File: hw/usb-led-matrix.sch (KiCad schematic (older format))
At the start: 79 parts, among them J1 Conn_01x04_Male, J2 Conn_ARM_JTAG_SWD_10, J3 USB_A, U1 AP1117-33, U2 stm32g473, U3 74LVT244A, Y1 Crystal_GND23

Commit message: Updates
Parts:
- removed U3: 74LVT244A, Package_SO:SOIC-20W_7.5x12.8mm_P1.27mm, symbol 74xx:74HC244
- added C1, C2, C3, C4, C7: C, Capacitor_SMD:C_0402_1005Metric_Pad0.74x0.62mm_HandSolder, symbol Device:C
- added C5, C6: C, Capacitor_SMD:C_0603_1608Metric_Pad1.08x0.95mm_HandSolder, symbol Device:C
- added R9: R, Resistor_SMD:R_0402_1005Metric_Pad0.72x0.64mm_HandSolder, symbol Device:R
- added U3: 74LVT245, Package_SO:TSSOP-20_4.4x6.5mm_P0.65mm, symbol 74xx:74LS245
- J1: footprint (none) -> Connector_PinHeader_1.27mm:PinHeader_1x04_P1.27mm_Vertical
- Y1: footprint (none) -> Crystal:Crystal_SMD_3225-4Pin_3.2x2.5mm_HandSoldering
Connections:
- net labels added: BOOT0, GND, NRST, RX, TX, VDD
- wire segments 244 -> 307
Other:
- note removed: "UART TX, RX, BOOT0, GND"
- moved on the sheet: J3, U1

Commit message: Work
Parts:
- removed J1: Conn_01x04_Male, Connector_PinHeader_1.27mm:PinHeader_1x04_P1.27mm_Vertical, symbol Connector:Conn_01x04_Male
- removed J2: Conn_ARM_JTAG_SWD_10, Connector_PinHeader_1.27mm:PinHeader_2x05_P1.27mm_Vertical, symbol Connector:Conn_ARM_JTAG_SWD_10
- removed Y1: Crystal_GND23, Crystal:Crystal_SMD_3225-4Pin_3.2x2.5mm_HandSoldering, symbol Device:Crystal_GND23
- added C8: C, Capacitor_SMD:C_0603_1608Metric_Pad1.08x0.95mm_HandSolder, symbol Device:C
- added C9: C, Capacitor_SMD:C_0402_1005Metric_Pad0.74x0.62mm_HandSolder, symbol Device:C
- added J2: Conn_ST_STDC14, Connector_PinHeader_1.27mm:PinHeader_2x07_P1.27mm_Vertical_SMD, symbol Connector:Conn_ST_STDC14
- added TP1, TP2, TP3: TestPoint, TestPoint:TestPoint_THTPad_D1.0mm_Drill0.5mm, symbol Connector:TestPoint
- added Y1: Crystal_GND24, Crystal:Crystal_SMD_3225-4Pin_3.2x2.5mm, symbol Device:Crystal_GND24
- J3: footprint (none) -> usb-board-edge:usb-a-board-edge
- U2: value stm32g473 -> STM32G473CET6
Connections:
- net labels added: VBUS
- wire segments 307 -> 316

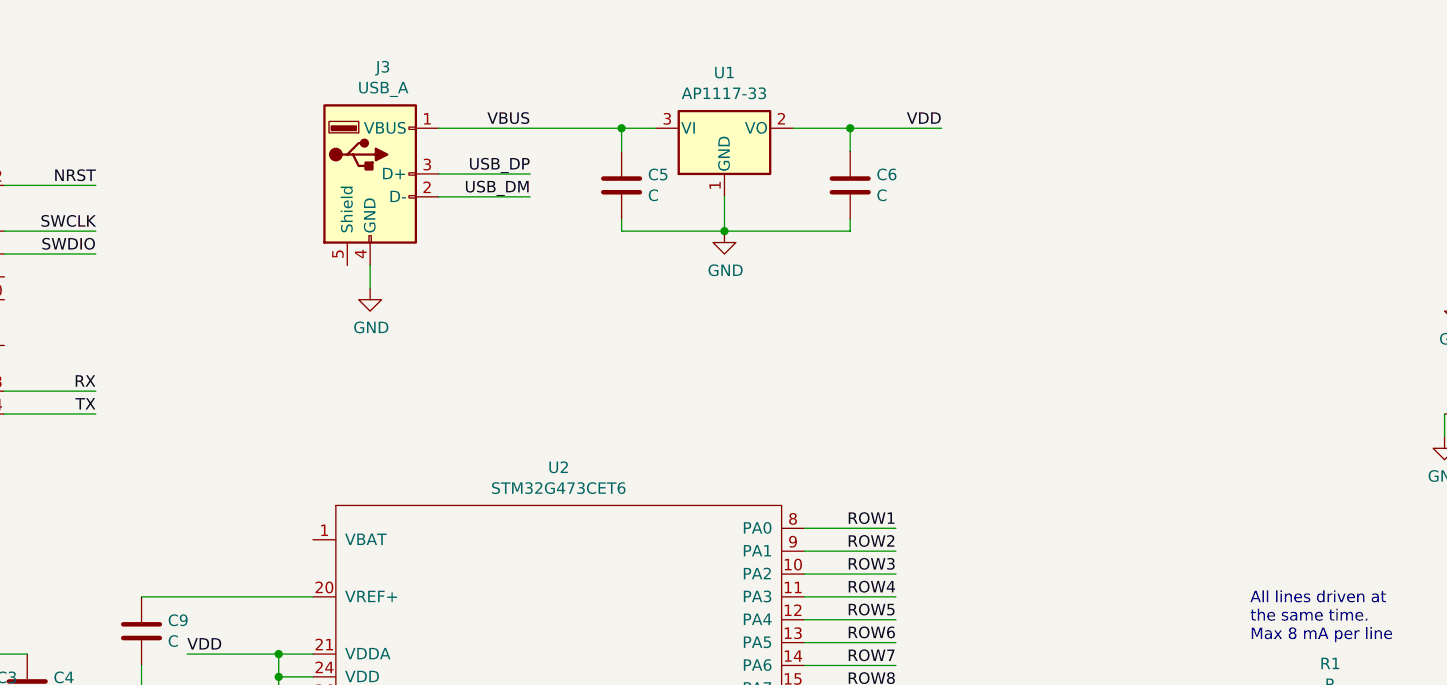
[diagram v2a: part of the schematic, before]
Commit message: USB-C connector
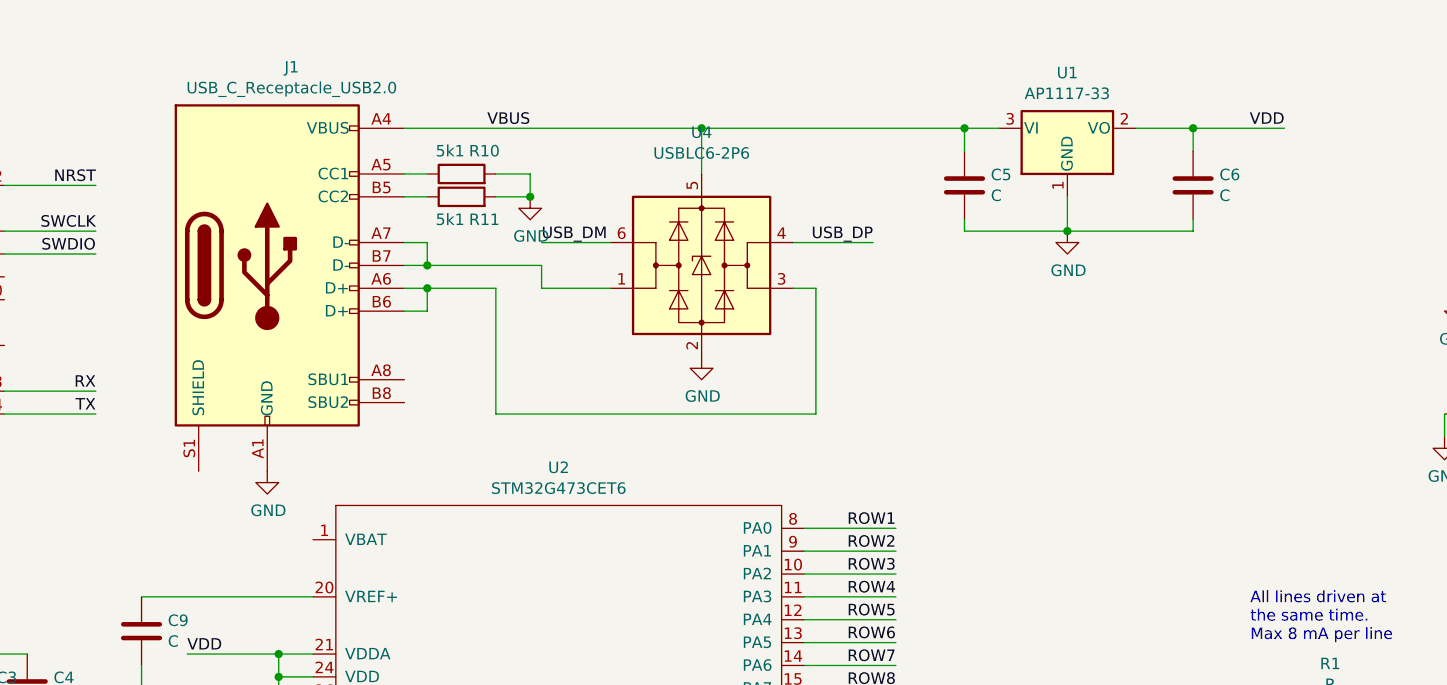
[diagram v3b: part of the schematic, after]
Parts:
- removed J3: USB_A, usb-board-edge:usb-a-board-edge, symbol Connector:USB_A
- added J1: USB_C_Receptacle_USB2.0, Connector_USB:USB_C_Receptacle_GCT_USB4085, symbol Connector:USB_C_Receptacle_USB2.0
- added R10, R11: 5k1, Resistor_SMD:R_0402_1005Metric_Pad0.72x0.64mm_HandSolder, symbol Device:R
- added U4: USBLC6-2P6, Package_TO_SOT_SMD:SOT-666, symbol Power_Protection:USBLC6-2P6
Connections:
- net GND: now also J1.A1 (GND), J1.A12 (GND), J1.B1 (GND), J1.B12 (GND), R10.2, R11.2, U4.2 (GND)
- net USB_DM: now also U4.6 (I/O1)
- net USB_DP: now also U4.4 (I/O2)
- net VBUS: now also J1.A4 (VBUS), J1.A9 (VBUS), J1.B4 (VBUS), J1.B9 (VBUS), U4.5 (VBUS)
- new net: J1.A5 (CC1), R10.1
- new net: J1.A6 (D+), J1.B6 (D+), U4.3 (I/O2)
- new net: J1.A7 (D-), J1.B7 (D-), U4.1 (I/O1)
- new net: J1.B5 (CC2), R11.1
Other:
- moved on the sheet: C5, C6, U1
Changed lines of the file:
@@
 L Regulator_Linear:AP1117-33 U1
 U 1 1 5FE78768
-P 5550 1100
-F 0 "U1" H 5550 1342 50  0000 C CNN
-F 1 "AP1117-33" H 5550 1251 50  0000 C CNN
-F 2 "Package_TO_SOT_SMD:SOT-223-3_TabPin2" H 5550 1300 50  0001 C CNN
-F 3 "http://www.diodes.com/datasheets/AP1117.pdf" H 5650 850 50  0001 C CNN
-	1    5550 1100
-	1    0    0    -1
-$EndComp
-$Comp
-L Connector:USB_A J3
-U 1 1 5FE79F29
-P 4000 1300
-F 0 "J3" H 4057 1767 50  0000 C CNN
-F 1 "USB_A" H 4057 1676 50  0000 C CNN
-F 2 "usb-board-edge:usb-a-board-edge" H 4150 1250 50  0001 C CNN
-F 3 " ~" H 4150 1250 50  0001 C CNN
-	1    4000 1300
+P 7050 1100
+F 0 "U1" H 7050 1342 50  0000 C CNN
+F 1 "AP1117-33" H 7050 1251 50  0000 C CNN
+F 2 "Package_TO_SOT_SMD:SOT-223-3_TabPin2" H 7050 1300 50  0001 C CNN
+F 3 "http://www.diodes.com/datasheets/AP1117.pdf" H 7150 850 50  0001 C CNN
+	1    7050 1100
 	1    0    0    -1
 $EndComp
@@
 Wire Wire Line
 	3600 5850 3750 5850
-Wire Wire Line
-	4300 1400 4700 1400
-Text Label 4700 1400 2    50   ~ 0
+Text Label 4750 1600 0    50   ~ 0
 USB_DM
-Text Label 4700 1300 2    50   ~ 0
+Text Label 6200 1600 2    50   ~ 0
 USB_DP
 Wire Wire Line
-	4300 1300 4700 1300
-Wire Wire Line
-	4300 1100 5100 1100
+	4150 1800 4250 1800
 $Comp
 L power:GND #PWR0103
 U 1 1 60097B36
-P 5550 1550
-F 0 "#PWR0103" H 5550 1300 50  0001 C CNN
-F 1 "GND" H 5555 1377 50  0000 C CNN
-F 2 "" H 5550 1550 50  0001 C CNN
-F 3 "" H 5550 1550 50  0001 C CNN
-	1    5550 1550
-	1    0    0    -1
-$EndComp
-Wire Wire Line
-	5550 1400 5550 1550
-Wire Wire Line
-	5850 1100 6100 1100
-Text Label 6500 1100 2    50   ~ 0
+P 7050 1550
+F 0 "#PWR0103" H 7050 1300 50  0001 C CNN
+F 1 "GND" H 7055 1377 50  0000 C CNN
+F 2 "" H 7050 1550 50  0001 C CNN
+F 3 "" H 7050 1550 50  0001 C CNN
+	1    7050 1550
+	1    0    0    -1
+$EndComp
+Wire Wire Line
+	7050 1400 7050 1550
+Wire Wire Line
+	7350 1100 7600 1100
+Text Label 8000 1100 2    50   ~ 0
 VDD
 Wire Wire Line
@@
 L Device:C C5
 U 1 1 60133436
-P 5100 1350
-F 0 "C5" H 5215 1396 50  0000 L CNN
-F 1 "C" H 5215 1305 50  0000 L CNN
-F 2 "Capacitor_SMD:C_0603_1608Metric_Pad1.08x0.95mm_HandSolder" H 5138 1200 50  0001 C CNN
-F 3 "~" H 5100 1350 50  0001 C CNN
-	1    5100 1350
+P 6600 1350
+F 0 "C5" H 6715 1396 50  0000 L CNN
+F 1 "C" H 6715 1305 50  0000 L CNN
+F 2 "Capacitor_SMD:C_0603_1608Metric_Pad1.08x0.95mm_HandSolder" H 6638 1200 50  0001 C CNN
+F 3 "~" H 6600 1350 50  0001 C CNN
+	1    6600 1350
 	1    0    0    -1
 $EndComp
@@
 L Device:C C6
 U 1 1 60134611
-P 6100 1350
-F 0 "C6" H 6215 1396 50  0000 L CNN
-F 1 "C" H 6215 1305 50  0000 L CNN
-F 2 "Capacitor_SMD:C_0603_1608Metric_Pad1.08x0.95mm_HandSolder" H 6138 1200 50  0001 C CNN
-F 3 "~" H 6100 1350 50  0001 C CNN
-	1    6100 1350
-	1    0    0    -1
-$EndComp
-Wire Wire Line
-	5100 1200 5100 1100
-Connection ~ 5100 1100
-Wire Wire Line
-	5100 1100 5250 1100
-Wire Wire Line
-	5100 1500 5100 1550
-Wire Wire Line
-	5100 1550 5550 1550
-Connection ~ 5550 1550
-Wire Wire Line
-	6100 1200 6100 1100
-Connection ~ 6100 1100
-Wire Wire Line
-	6100 1100 6500 1100
-Wire Wire Line
-	6100 1500 6100 1550
-Wire Wire Line
-	6100 1550 5550 1550
+P 7600 1350
+F 0 "C6" H 7715 1396 50  0000 L CNN
+F 1 "C" H 7715 1305 50  0000 L CNN
+F 2 "Capacitor_SMD:C_0603_1608Metric_Pad1.08x0.95mm_HandSolder" H 7638 1200 50  0001 C CNN
+F 3 "~" H 7600 1350 50  0001 C CNN
+	1    7600 1350
+	1    0    0    -1
+$EndComp
+Wire Wire Line
+	6600 1200 6600 1100
+Wire Wire Line
+	6600 1100 6750 1100
+Wire Wire Line
+	6600 1500 6600 1550
+Wire Wire Line
+	6600 1550 7050 1550
+Connection ~ 7050 1550
+Wire Wire Line
+	7600 1200 7600 1100
+Connection ~ 7600 1100
+Wire Wire Line
+	7600 1100 8000 1100
+Wire Wire Line
+	7600 1500 7600 1550
+Wire Wire Line
+	7600 1550 7050 1550
 $Comp
 L Device:C C4
@@
 L power:GND #PWR0108
 U 1 1 60481ABB
-P 4000 1800
-F 0 "#PWR0108" H 4000 1550 50  0001 C CNN
-F 1 "GND" H 4005 1627 50  0000 C CNN
-F 2 "" H 4000 1800 50  0001 C CNN
-F 3 "" H 4000 1800 50  0001 C CNN
-	1    4000 1800
-	1    0    0    -1
-$EndComp
-Wire Wire Line
-	4000 1700 4000 1800
+P 3550 2600
+F 0 "#PWR0108" H 3550 2350 50  0001 C CNN
+F 1 "GND" H 3555 2427 50  0000 C CNN
+F 2 "" H 3550 2600 50  0001 C CNN
+F 3 "" H 3550 2600 50  0001 C CNN
+	1    3550 2600
+	1    0    0    -1
+$EndComp
 Text Label 4700 1100 2    50   ~ 0
 VBUS
@@
 	1    0    0    -1
 $EndComp
+$Comp
+L Connector:USB_C_Receptacle_USB2.0 J1
+U 1 1 5FF05986
+P 3550 1700
+F 0 "J1" H 3657 2567 50  0000 C CNN
+F 1 "USB_C_Receptacle_USB2.0" H 3657 2476 50  0000 C CNN
+F 2 "Connector_USB:USB_C_Receptacle_GCT_USB4085" H 3700 1700 50  0001 C CNN
+F 3 "https://www.usb.org/sites/default/files/documents/usb_type-c.zip" H 3700 1700 50  0001 C CNN
+	1    3550 1700
+	1    0    0    -1
+$EndComp
+Wire Wire Line
+	4150 1600 4250 1600
+Wire Wire Line
+	4150 1700 4250 1700
+Wire Wire Line
+	4250 1700 4250 1600
+Wire Wire Line
+	4250 1800 4250 1900
+Wire Wire Line
+	4250 1900 4150 1900
+Connection ~ 4250 1800
+Wire Wire Line
+	4250 1800 4550 1800
+$Comp
+L Device:R R10
+U 1 1 5FFDAC01
+P 4400 1300
+F 0 "R10" V 4500 1200 50  0000 C CNN
+F 1 "5k1" V 4500 1350 50  0000 C CNN
+F 2 "Resistor_SMD:R_0402_1005Metric_Pad0.72x0.64mm_HandSolder" V 4330 1300 50  0001 C CNN
+F 3 "~" H 4400 1300 50  0001 C CNN
+	1    4400 1300
+	0    -1   -1   0
+$EndComp
+$Comp
+L Device:R R11
+U 1 1 60024C32
+P 4400 1400
+F 0 "R11" V 4300 1300 50  0000 C CNN
+F 1 "5k1" V 4300 1450 50  0000 C CNN
+F 2 "Resistor_SMD:R_0402_1005Metric_Pad0.72x0.64mm_HandSolder" V 4330 1400 50  0001 C CNN
+F 3 "~" H 4400 1400 50  0001 C CNN
+	1    4400 1400
+	0    -1   -1   0
+$EndComp
+$Comp
+L power:GND #PWR0113
+U 1 1 6006E538
+P 4700 1400
+F 0 "#PWR0113" H 4700 1150 50  0001 C CNN
+F 1 "GND" H 4705 1227 50  0000 C CNN
+F 2 "" H 4700 1400 50  0001 C CNN
+F 3 "" H 4700 1400 50  0001 C CNN
+	1    4700 1400
+	1    0    0    -1
+$EndComp
+$Comp
+L Power_Protection:USBLC6-2P6 U4
+U 1 1 600BA695
+P 5450 1700
+F 0 "U4" H 5450 2281 50  0000 C CNN
+F 1 "USBLC6-2P6" H 5450 2190 50  0000 C CNN
+F 2 "Package_TO_SOT_SMD:SOT-666" H 5450 1200 50  0001 C CNN
+F 3 "https://www.st.com/resource/en/datasheet/usblc6-2.pdf" H 5650 2050 50  0001 C CNN
+	1    5450 1700
+	1    0    0    -1
+$EndComp
+Wire Wire Line
+	4550 1400 4700 1400
+Wire Wire Line
+	4700 1400 4700 1300
+Wire Wire Line
+	4550 1300 4700 1300
+Connection ~ 4700 1400
+Wire Wire Line
+	4250 1300 4150 1300
+Wire Wire Line
+	4150 1400 4250 1400
+$Comp
+L power:GND #PWR0114
+U 1 1 601C595C
+P 5450 2100
+F 0 "#PWR0114" H 5450 1850 50  0001 C CNN
+F 1 "GND" H 5455 1927 50  0000 C CNN
+F 2 "" H 5450 2100 50  0001 C CNN
+F 3 "" H 5450 2100 50  0001 C CNN
+	1    5450 2100
+	1    0    0    -1
+$EndComp
+Wire Wire Line
+	4150 1100 5450 1100
+Wire Wire Line
+	5450 1100 5450 1300
+Wire Wire Line
+	4750 1800 5050 1800
+Wire Wire Line
+	4550 1800 4550 2350
+Wire Wire Line
+	4550 2350 5950 2350
+Wire Wire Line
+	4750 1800 4750 1700
+Wire Wire Line
+	4750 1700 4250 1700
+Connection ~ 4250 1700
+Wire Wire Line
+	5950 2350 5950 1800
+Wire Wire Line
+	5950 1800 5850 1800
+Wire Wire Line
+	5850 1600 6200 1600
+Wire Wire Line
+	5050 1600 4750 1600
+Wire Wire Line
+	6600 1100 5450 1100
+Connection ~ 6600 1100
+Connection ~ 5450 1100
 $EndSCHEMATC

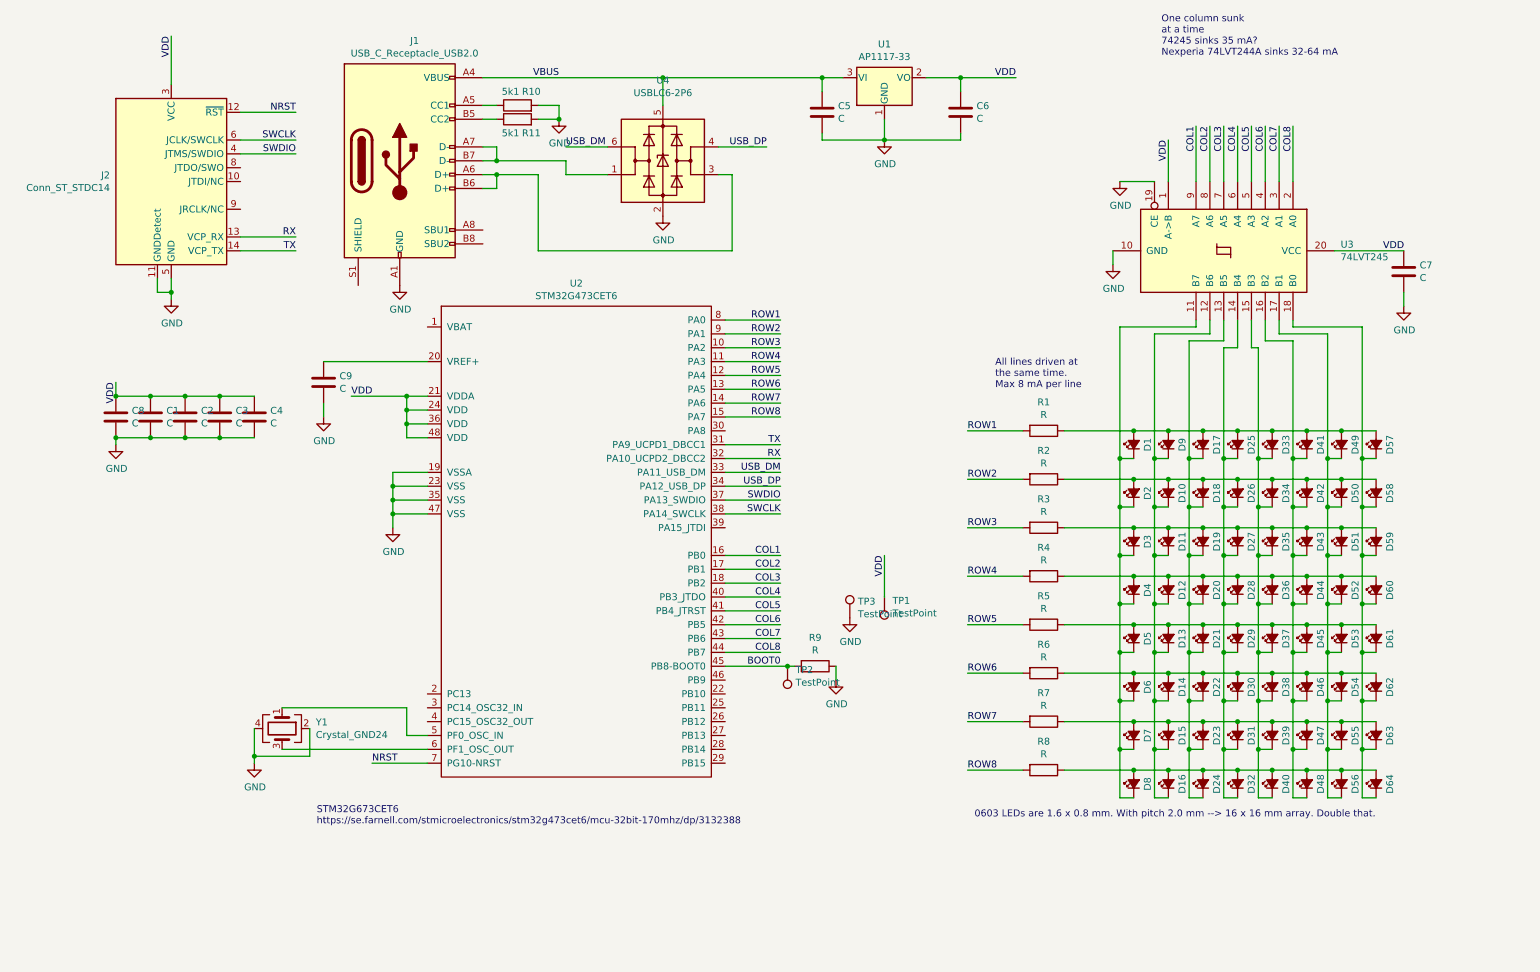
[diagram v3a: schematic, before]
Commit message: Schematic updates
- TVS on USB
- SOT23-5 vreg
- 100n on NRST
- SWO hooked up
- Caps on crystal
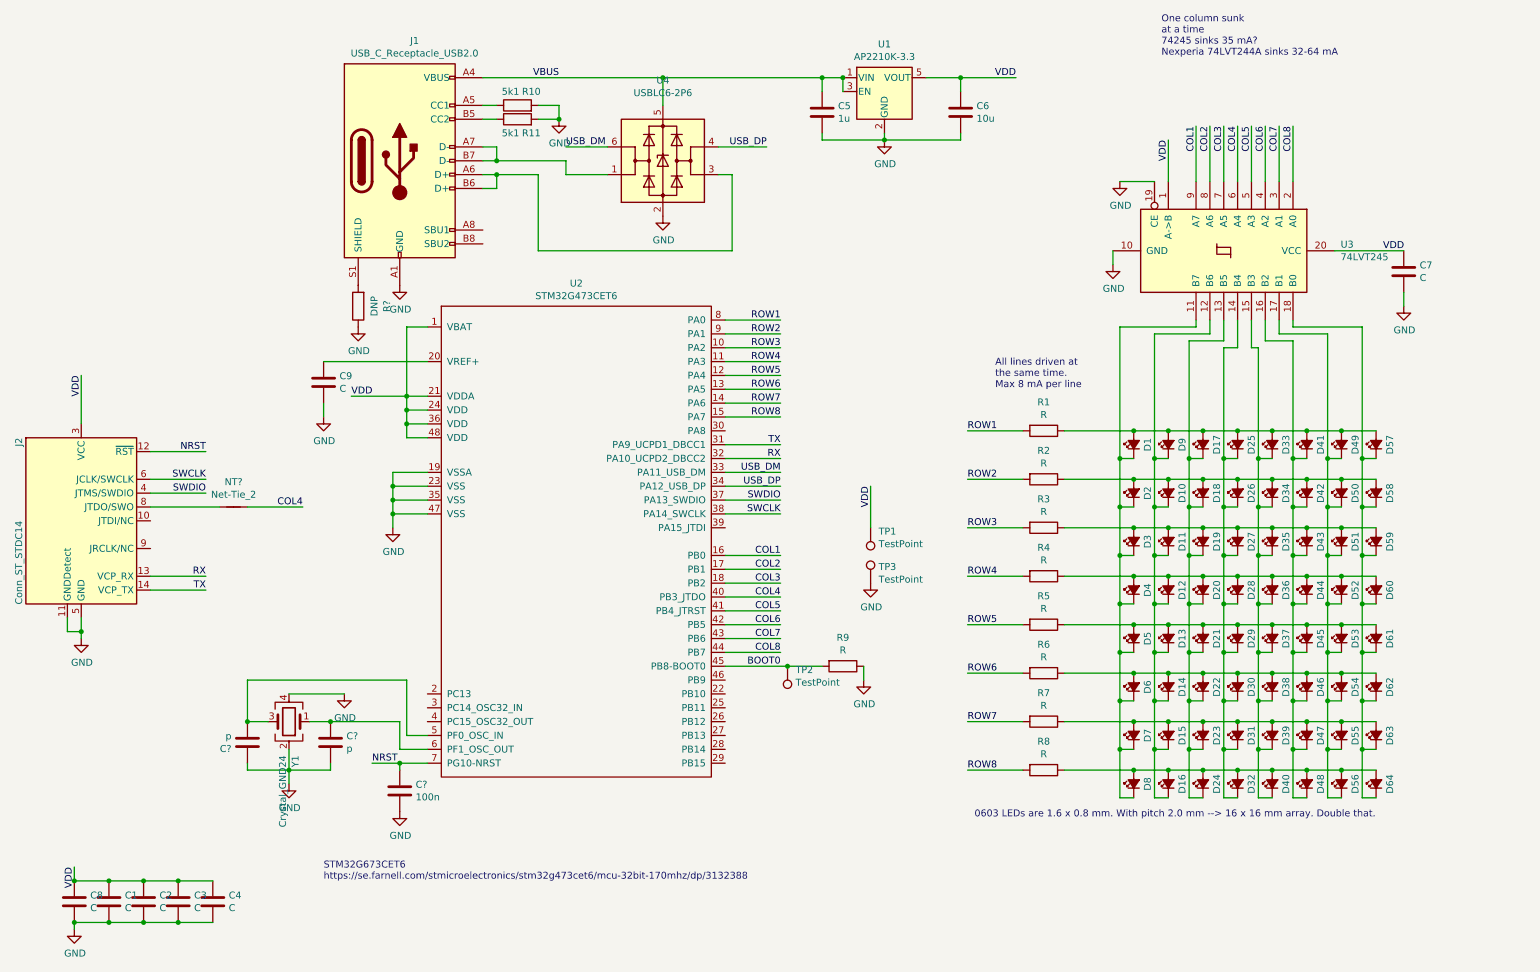
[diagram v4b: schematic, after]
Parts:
- removed U1: AP1117-33, Package_TO_SOT_SMD:SOT-223-3_TabPin2, symbol Regulator_Linear:AP1117-33
- added C?: 100n, Capacitor_SMD:C_0402_1005Metric_Pad0.74x0.62mm_HandSolder, symbol Device:C
- added C? (x2): p, Capacitor_SMD:C_0402_1005Metric_Pad0.74x0.62mm_HandSolder, symbol Device:C
- added NT?: Net-Tie_2, symbol Device:Net-Tie_2
- added R?: DNP, Resistor_SMD:R_0402_1005Metric_Pad0.72x0.64mm_HandSolder, symbol Device:R
- added U1: AP2210K-3.3, Package_TO_SOT_SMD:SOT-23-5, symbol Regulator_Linear:AP2204K-3.3
- C5: value C -> 1u
- C6: value C -> 10u
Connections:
- net COL4: now also NT?.2
- net GND: now also C?.1, C?.2, C?.2, R?.1, U1.2 (GND)
- net NRST: now also C?.1
- net VBUS: now also U1.1 (VIN), U1.3 (EN)
- net VDD: now also U2.1 (VBAT), U1.5 (VOUT)
- net at J1.S1 (SHIELD): now also R?.2
- net at Y1.1: now also U2.6 (PF1_OSC_OUT), C?.1; no longer U2.5 (PF0_OSC_IN)
- net at Y1.3: now also U2.5 (PF0_OSC_IN), C?.2; no longer U2.6 (PF1_OSC_OUT)
- net at J2.8 (JTDO/SWO): now also NT?.1
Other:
- moved on the sheet: C1, C2, C3, C4, C8, J2, R9, TP1, TP3, Y1

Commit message: Connect more USB signals
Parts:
- added NT2, NT3: Net-Tie_2, NetTie:NetTie-2_SMD_Pad0.5mm, symbol Device:Net-Tie_2
- added TP4, TP5: TestPoint, TestPoint:TestPoint_Pad_1.0x1.0mm, symbol Connector:TestPoint
- NT1: renamed from NT?; footprint (none) -> NetTie:NetTie-2_SMD_Pad0.5mm
- gave numbers to parts that had none: 4
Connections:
- net GND: now also R11.1; no longer R11.2
- net RX: now also U2.22 (PB10); no longer U2.32 (PA10_UCPD2_DBCC2)
- net TX: now also U2.25 (PB11); no longer U2.31 (PA9_UCPD1_DBCC1)
- net VBUS: no longer C5.1, J1.A4 (VBUS), J1.A9 (VBUS), J1.B4 (VBUS), J1.B9 (VBUS), U1.1 (VIN), U1.3 (EN), U4.5 (VBUS)
- net at J1.A5 (CC1): now also R11.2, NT2.1; no longer R10.1
- net at J1.A8 (SBU1): now also TP4.1
- net at J1.B5 (CC2): now also R10.1, NT3.1; no longer R11.1
- net at J1.B8 (SBU2): now also TP5.1
- new net: C5.1, U1.1 (VIN), U1.3 (EN), U4.5 (VBUS)
- new net: J1.A4 (VBUS), J1.A9 (VBUS), J1.B4 (VBUS), J1.B9 (VBUS)
- new net USB_CC1: NT2.2, U2.31 (PA9_UCPD1_DBCC1)
- new net USB_CC2: NT3.2, U2.32 (PA10_UCPD2_DBCC2)
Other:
- note added: "LPUART1"
- note added: "STM32G473CET6\nhttps://se.farnell.com/stmicroelectronics/stm32g473cet6/mcu-32bit-170mhz/dp/3132388"
- note removed: "STM32G673CET6\nhttps://se.farnell.com/stmicroelectronics/stm32g473cet6/mcu-32bit-170mhz/dp/3132388"
- moved on the sheet: J1, R10, R11, R12
